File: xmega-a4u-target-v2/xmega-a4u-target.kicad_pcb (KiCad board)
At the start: 2 copper layers, 50.8 x 17.8 mm, 48 parts, among them CON1 USB-MINI-B, IC1 ATXMEGA128A4U-M, P1 PORT E, P2 PORT D, P3 PORT A, P4 PORT B, P5 PORT C, P6 PWR/RST, P7 PDI, U1 TSX-3225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

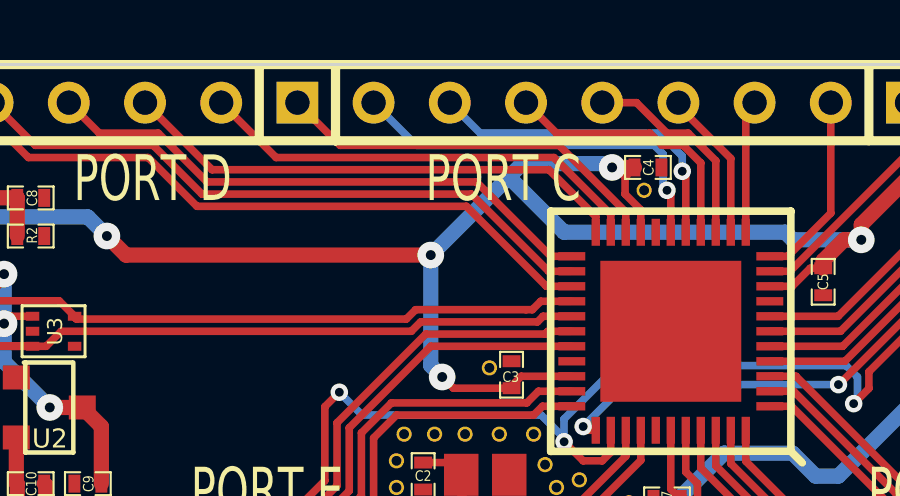
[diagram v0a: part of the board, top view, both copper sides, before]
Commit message: adjusted a drill position i didn't like
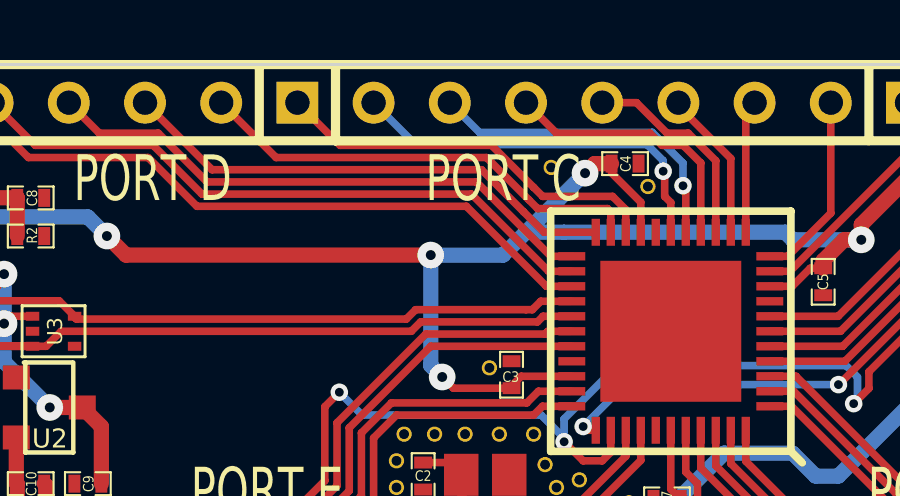
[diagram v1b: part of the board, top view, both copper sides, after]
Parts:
- added HOLE: VAL**, HOLE, F.Cu at (179.9, 79.6)
- moved C4 0.77 mm to (182.4, 79.5)
- moved HOLE 0.18 mm to (183.1, 80.3)
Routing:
- net VCC: track 84.3 -> 82.4 mm

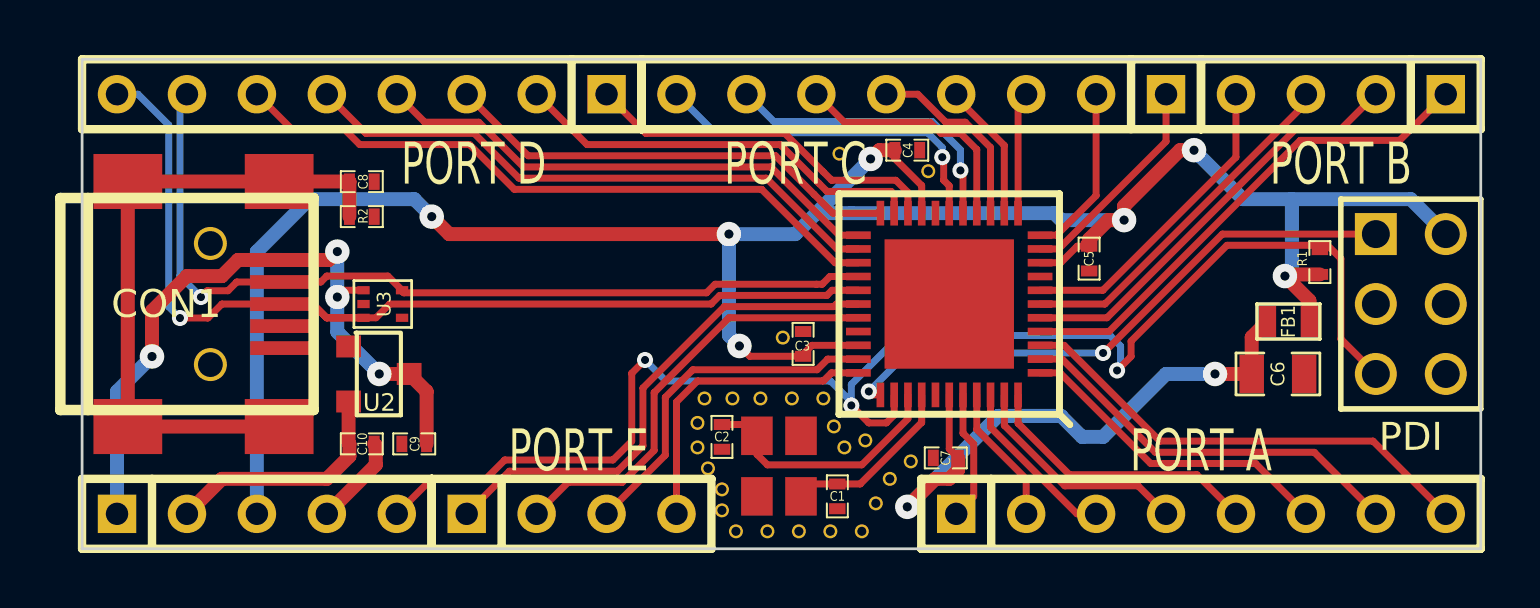
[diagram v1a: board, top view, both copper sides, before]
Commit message: moar holes plz
(added more ground connections on a4u board, around areas that i suspect are especially sensitive or noisy... no idea whether it's actually a valuable thing to do though, i'm just cargo culting here ;))
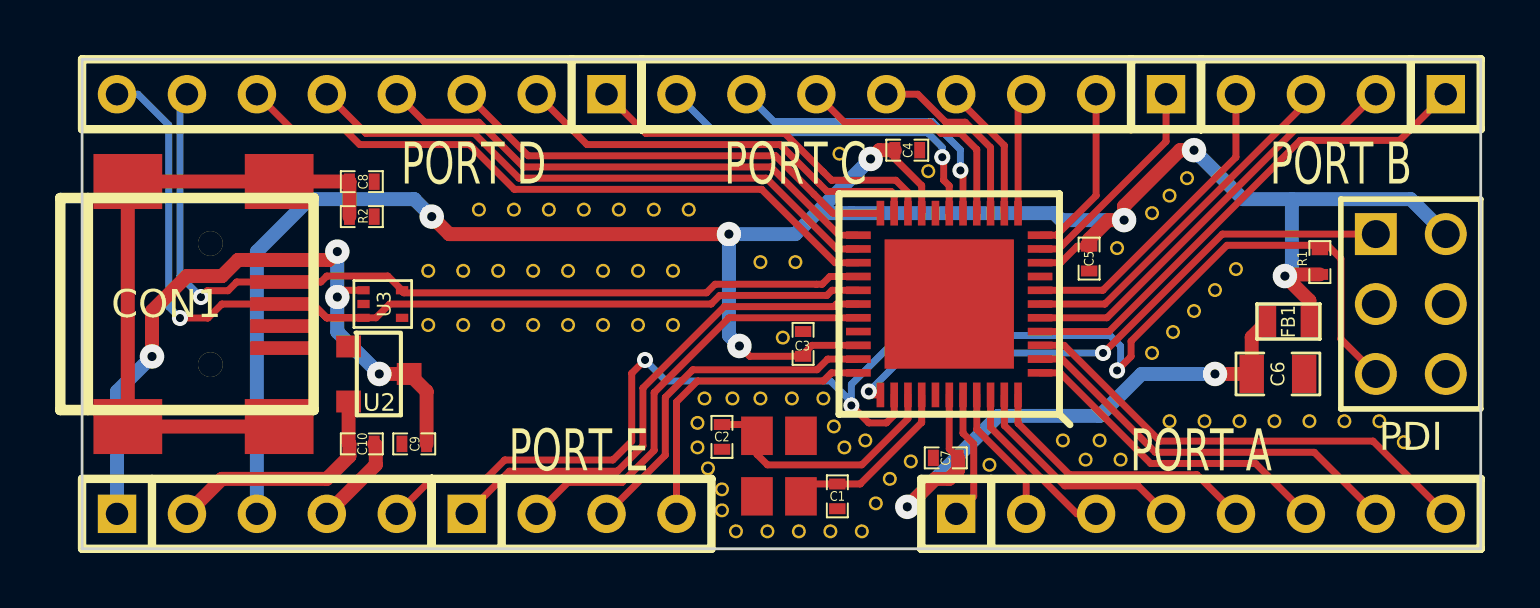
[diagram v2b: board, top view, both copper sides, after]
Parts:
- added HOLE: VAL**, HOLE, F.Cu at (188.0, 90.0)
- added HOLE: VAL**, HOLE, F.Cu at (197.0, 89.3)
- added HOLE: VAL**, HOLE, F.Cu at (198.2, 89.3)
- added HOLE: VAL**, HOLE, F.Cu at (200.4, 90.1)
- added HOLE: VAL**, HOLE, F.Cu at (199.5, 89.3)
- added HOLE: VAL**, HOLE, F.Cu at (191.9, 81.2)
- added HOLE: VAL**, HOLE, F.Cu at (190.0, 83.1)
- added HOLE: VAL**, HOLE, F.Cu at (192.5, 80.5)
- added HOLE: VAL**, HOLE, F.Cu at (191.3, 81.8)
- added HOLE: VAL**, HOLE, F.Cu at (191.3, 86.9)
- added HOLE: VAL**, HOLE, F.Cu at (193.5, 84.6)
- added HOLE: VAL**, HOLE, F.Cu at (189.4, 90.0)
- added HOLE: VAL**, HOLE, F.Cu at (194.3, 83.8)
- added HOLE: VAL**, HOLE, F.Cu at (192.8, 85.3)
- added HOLE: VAL**, HOLE, F.Cu at (192.0, 86.1)
- added HOLE: VAL**, HOLE, F.Cu at (168.1, 81.7)
- added HOLE: VAL**, HOLE, F.Cu at (169.4, 81.7)
- added HOLE: VAL**, HOLE, F.Cu at (166.8, 81.7)
- added HOLE: VAL**, HOLE, F.Cu at (170.6, 81.7)
- added HOLE: VAL**, HOLE, F.Cu at (171.9, 81.7)
- added HOLE: VAL**, HOLE, F.Cu at (174.4, 81.7)
- added HOLE: VAL**, HOLE, F.Cu at (173.2, 81.7)
- added HOLE: VAL**, HOLE, F.Cu at (185.4, 90.9)
- added HOLE: VAL**, HOLE, F.Cu at (178.3, 83.6)
- added HOLE: VAL**, HOLE, F.Cu at (177.0, 83.6)
- added HOLE: VAL**, HOLE, F.Cu at (167.5, 85.9)
- added HOLE: VAL**, HOLE, F.Cu at (168.8, 85.9)
- added HOLE: VAL**, HOLE, F.Cu at (166.2, 85.9)
- added HOLE: VAL**, HOLE, F.Cu at (165.0, 85.9)
- added HOLE: VAL**, HOLE, F.Cu at (170.1, 85.9)
- added HOLE: VAL**, HOLE, F.Cu at (171.3, 85.9)
- added HOLE: VAL**, HOLE, F.Cu at (173.9, 85.9)
- added HOLE: VAL**, HOLE, F.Cu at (172.6, 85.9)
- added HOLE: VAL**, HOLE, F.Cu at (188.8, 90.7)
- added HOLE: VAL**, HOLE, F.Cu at (172.6, 83.9)
- added HOLE: VAL**, HOLE, F.Cu at (173.9, 83.9)
- added HOLE: VAL**, HOLE, F.Cu at (171.3, 83.9)
- added HOLE: VAL**, HOLE, F.Cu at (170.1, 83.9)
- added HOLE: VAL**, HOLE, F.Cu at (165.0, 83.9)
- added HOLE: VAL**, HOLE, F.Cu at (166.2, 83.9)
- added HOLE: VAL**, HOLE, F.Cu at (168.8, 83.9)
- added HOLE: VAL**, HOLE, F.Cu at (190.1, 90.7)
- added HOLE: VAL**, HOLE, F.Cu at (194.4, 89.3)
- added HOLE: VAL**, HOLE, F.Cu at (195.7, 89.3)
- added HOLE: VAL**, HOLE, F.Cu at (167.5, 83.9)
- added HOLE: VAL**, HOLE, F.Cu at (193.2, 89.3)
- added HOLE: VAL**, HOLE, F.Cu at (191.9, 89.3)
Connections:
- CON1 pad : GND -> (no net)
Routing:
- net AVCC: track 22.5 -> 21.9 mm

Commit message: fixed a mistake on XMEGA A4U board
one of the crystal's ground pads was not connected on the schematic
(the lines were "touching" but not actually connected)
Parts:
- P1: value PORT E -> PORTE
- P2: value PORT D -> PORTD
- P3: value PORT A -> PORTA
- P4: value PORT B -> PORTB
- P5: value PORT C -> PORTC
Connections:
- U1 pad 2: (no net) -> GND

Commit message: embiggened pin header drill holes on A4U board...
... and added a VREG-VCC jumper
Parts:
- added JP1: JUMPER, SM0603, F.Cu at (156.8, 90.6)
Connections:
- IC1 pad 45: GND -> (no net)
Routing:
- net VCC: track 82.4 -> 87.5 mm, vias 7 -> 8
- net VREG: track 8.77 -> 9.46 mm
